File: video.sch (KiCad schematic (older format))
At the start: 32 parts, among them CN10 COMPOSITE, CN9 VIDEO_DB23M, U4 DENISE, U40 74LS245, U41 74LS245

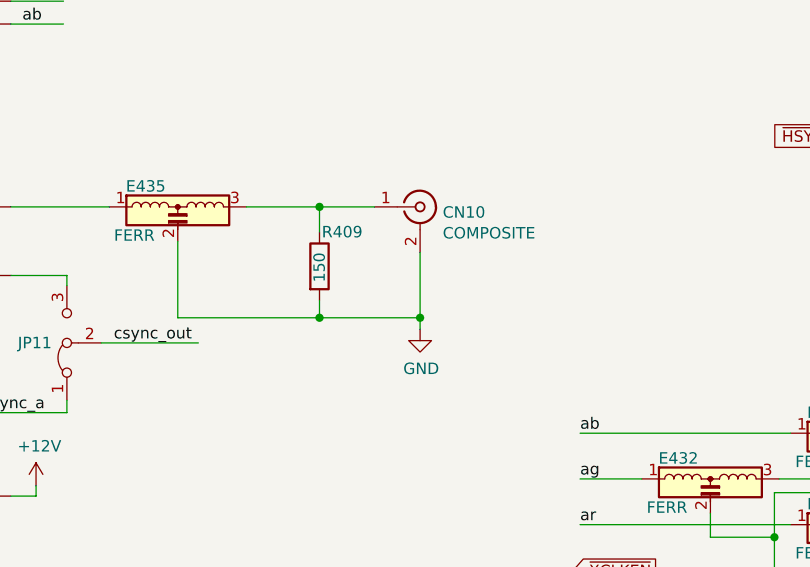
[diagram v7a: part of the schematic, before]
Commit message: Replace audio/composite jacks with A600's - This means PCB IS READY! Still need to fix the silkscreen though...
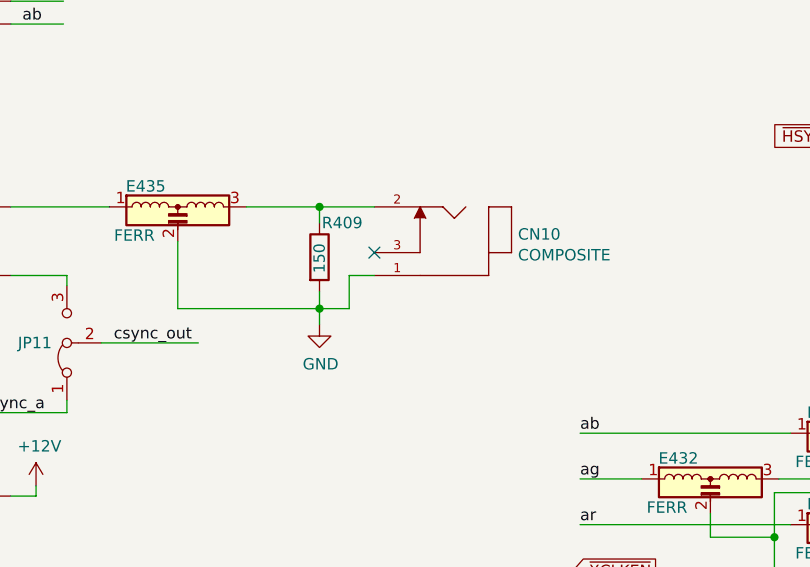
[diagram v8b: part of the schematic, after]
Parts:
- removed CN10: COMPOSITE, w_conn_av:rca_yellow, symbol Connector:Conn_Coaxial
- added CN10: COMPOSITE, Raemixx500:SWITCHCRAFT_PJRAN1X1U01X, symbol PJRAN1X1U01X:PJRAN1X1U01X
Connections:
- wire segments 316 -> 317
- no-connect marks 0 -> 1
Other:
- moved on the sheet: R409
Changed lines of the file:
@@
 Sheet 4 14
 Title "Rämixx500"
-Date "2019-05-11"
+Date "2020-04-05"
 Rev "1git"
 Comp "SukkoPera"
@@
 rbcsync_a
 $Comp
-L Connector:Conn_Coaxial CN?
-U 1 1 5D9B0BDD
-P 10180 3975
-AR Path="/5D2DC3A1/5D9B0BDD" Ref="CN?"  Part="1"
-AR Path="/5CBA5669/5D9B0BDD" Ref="CN10"  Part="1"
-F 0 "CN10" H 10279 3951 50  0000 L CNN
-F 1 "COMPOSITE" H 10279 3860 50  0000 L CNN
-F 2 "w_conn_av:rca_yellow" H 10180 3975 50  0001 C CNN
-F 3 " ~" H 10180 3975 50  0001 C CNN
-	1    10180 3975
-	1    0    0    -1
-$EndComp
-$Comp
 L power:GND #PWR0264
 U 1 1 5D9F0427
-P 10180 4510
-F 0 "#PWR0264" H 10180 4260 50  0001 C CNN
-F 1 "GND" H 10185 4337 50  0000 C CNN
-F 2 "" H 10180 4510 50  0001 C CNN
-F 3 "" H 10180 4510 50  0001 C CNN
-	1    10180 4510
-	1    0    0    -1
-$EndComp
-Wire Wire Line
-	10180 4510 10180 4460
+P 9740 4490
+F 0 "#PWR0264" H 9740 4240 50  0001 C CNN
+F 1 "GND" H 9745 4317 50  0000 C CNN
+F 2 "" H 9740 4490 50  0001 C CNN
+F 3 "" H 9740 4490 50  0001 C CNN
+	1    9740 4490
+	1    0    0    -1
+$EndComp
 $Comp
 L Device:R R409
 U 1 1 5DA05B94
-P 9740 4235
-F 0 "R409" H 9750 4385 50  0000 L CNN
-F 1 "150" V 9740 4165 50  0000 L CNN
-F 2 "Raemixx500:C_Axial_L9.0mm_D3.2mm_P12.70mm" V 9670 4235 50  0001 C CNN
-F 3 "~" H 9740 4235 50  0001 C CNN
-	1    9740 4235
-	1    0    0    -1
-$EndComp
-Wire Wire Line
-	9740 4385 9740 4460
-Connection ~ 10180 4460
-Wire Wire Line
-	10180 4460 10180 4175
-Wire Wire Line
-	9740 4085 9740 3975
+P 9740 4195
+F 0 "R409" H 9750 4345 50  0000 L CNN
+F 1 "150" V 9740 4125 50  0000 L CNN
+F 2 "Raemixx500:C_Axial_L9.0mm_D3.2mm_P12.70mm" V 9670 4195 50  0001 C CNN
+F 3 "~" H 9740 4195 50  0001 C CNN
+	1    9740 4195
+	1    0    0    -1
+$EndComp
+Wire Wire Line
+	9740 4345 9740 4420
+Wire Wire Line
+	9740 4045 9740 3975
 Connection ~ 9740 3975
 Wire Wire Line
@@
 $EndComp
 Wire Wire Line
-	9120 4125 9120 4460
-Wire Wire Line
-	9120 4460 9740 4460
-Connection ~ 9740 4460
-Wire Wire Line
-	9740 4460 10180 4460
+	9120 4125 9120 4420
+Wire Wire Line
+	9120 4420 9740 4420
+Connection ~ 9740 4420
+Wire Wire Line
+	9740 4420 9870 4420
 $Comp
 L power:PWR_FLAG #FLG0101
@@
 Wire Wire Line
 	14125 825  14125 745
+$Comp
+L PJRAN1X1U01X:PJRAN1X1U01X CN?
+U 1 1 5FB5AA2B
+P 10280 4175
+AR Path="/5D2DC3A1/5FB5AA2B" Ref="CN?"  Part="1"
+AR Path="/5CBA5669/5FB5AA2B" Ref="CN10"  Part="1"
+F 0 "CN10" H 9952 4255 50  0000 R CNN
+F 1 "COMPOSITE" H 9952 4164 50  0000 R CNN
+F 2 "Raemixx500:SWITCHCRAFT_PJRAN1X1U01X" H 10280 4175 50  0001 L BNN
+F 3 "A" H 10280 4175 50  0001 L BNN
+F 4 "Switchcraft" H 10280 4175 50  0001 L BNN "Field4"
+F 5 "13mm" H 10280 4175 50  0001 L BNN "Field5"
+F 6 "Manufacturer Recommendations" H 10280 4175 50  0001 L BNN "Field6"
+	1    10280 4175
+	-1   0    0    -1
+$EndComp
+NoConn ~ 9980 4175
+Wire Wire Line
+	9980 4275 9870 4275
+Wire Wire Line
+	9870 4275 9870 4420
+Wire Wire Line
+	9740 4420 9740 4490
 Wire Bus Line
 	2005 3775 2005 4475
